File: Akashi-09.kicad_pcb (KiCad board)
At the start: 2 copper layers, 68.6 x 53.3 mm, 46 parts, among them J1 9-1437539-2, P1 Power, P2 Analog, P3 Digital, P4 Digital, P5 CONN_01X01, P6 CONN_01X01, P7 CONN_01X01, P8 CONN_01X01, SW1 SW_MEC_5G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

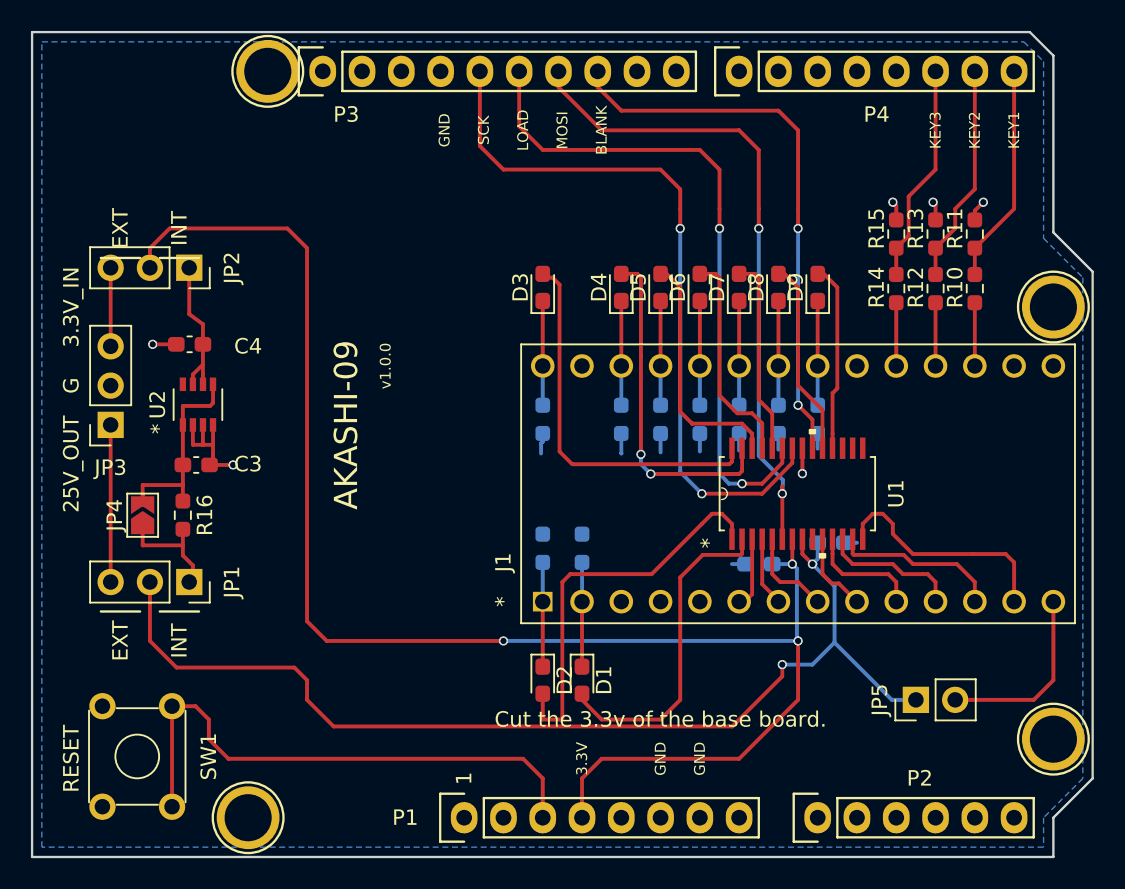
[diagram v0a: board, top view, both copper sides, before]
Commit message: Add test point
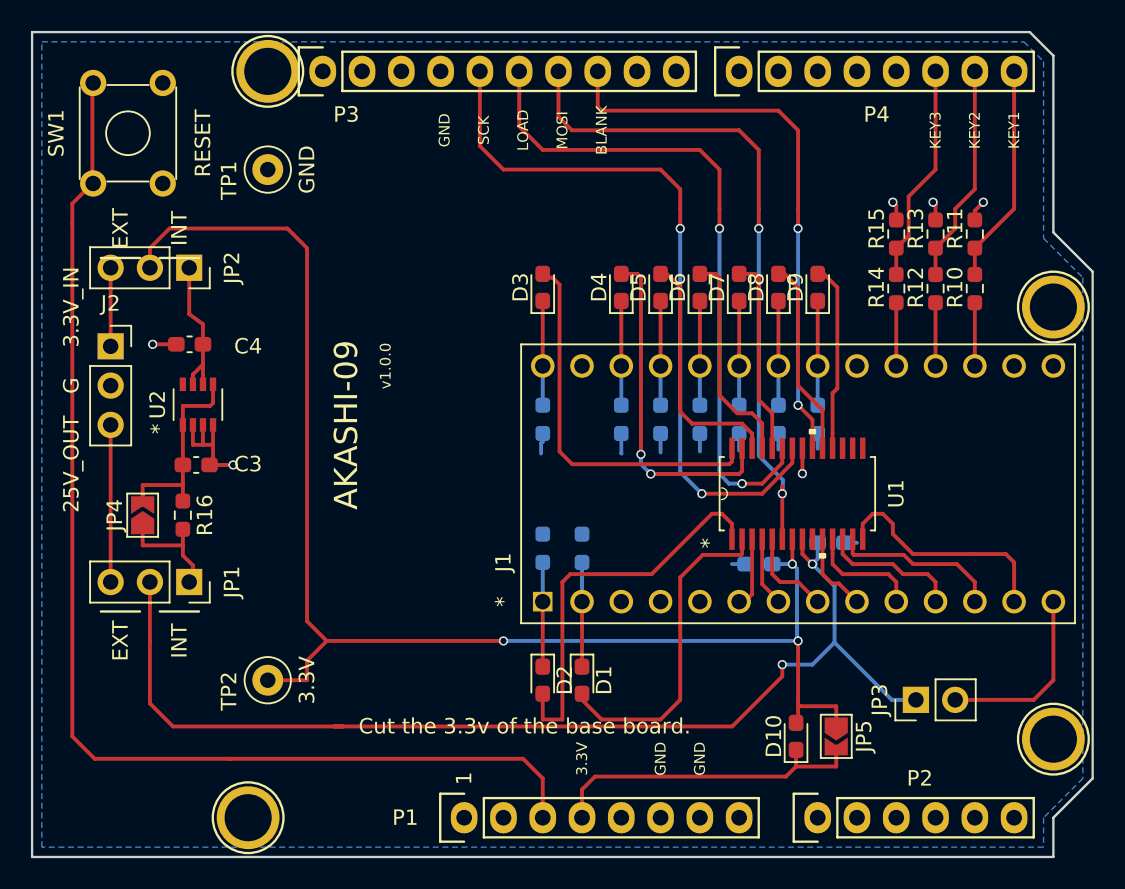
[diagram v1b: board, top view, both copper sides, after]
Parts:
- removed the JP3 at (116.1, 98.4)
- added D10: D, Diode_SMD:D_0603_1608Metric_Pad1.05x0.95mm_HandSolder, F.Cu at (160.4, 118.6)
- added J2: Conn_01x03_Male, Connector_PinSocket_2.54mm:PinSocket_1x03_P2.54mm_Vertical, F.Cu at (116.1, 93.3)
- added JP5: SolderJumper_2_Open, Jumper:SolderJumper-2_P1.3mm_Open_TrianglePad1.0x1.5mm, F.Cu at (163.0, 118.6)
- added TP1: TestPoint, TestPoint:TestPoint_Loop_D1.80mm_Drill1.0mm_Beaded, F.Cu at (126.2, 81.9)
- added TP2: TestPoint, TestPoint:TestPoint_Loop_D1.80mm_Drill1.0mm_Beaded, F.Cu at (126.2, 114.9)
- R16: value R -> 1k
- moved SW1 47.0 mm to (119.4, 76.3), turned to 270 degrees
- renumbered JP5 to JP3
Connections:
- P1 pad 4: +3V3 -> /BASE_3.3V
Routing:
- net /nRESET: track 35.6 -> 77.0 mm
- net /BASE_3.3V: track 0.00 -> 21.3 mm
- net +3V3: track 99.3 -> 91.9 mm
- net /VBB: track 69.9 -> 72.2 mm
- net /MOSI: track 42.4 -> 43.5 mm
- net /BLANK: track 36.1 -> 36.8 mm
